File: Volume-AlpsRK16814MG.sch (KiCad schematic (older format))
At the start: 7 parts, among them P1 AB I/O, P2 CD I/O, P3 VD, P4 CTRL, U1 SN754410

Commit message: Flooded.
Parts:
- added P5: GND, mfk-AVA-20ga, symbol CONN_1
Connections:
- net GND: now also P5.1
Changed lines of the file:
@@
 63 98 05 E1 6B C4 72 91 8E EA 95 27 8C 4B 0B 6B 30 6B 95 2D 08 DF 47 79 14 D8 40 20 A9 90 96 2D
 E1 E7 3D C6 74 F3 E0 6E B9 00 E4 0E CC EC 2A 00 9E 03 F9 2E 43 53 93 3B E7 B1 3D FE 0F E4 2C B5
-B8 3A B8 3B 5D 00 00 00 00 49 45 4E 44 AE 42 60 82 C2 $EndBitmap
+B8 3A B8 3B 5D 00 00 00 00 49 45 4E 44 AE 42 60 82 AB $EndBitmap
 EndData
 $EndBitmap
@@
 Wire Wire Line
 	4700 6000 4700 6100
+$Comp
+L CONN_1 P5
+U 1 1 550D1AD1
+P 4350 6000
+F 0 "P5" H 4430 6000 40  0000 L CNN
+F 1 "GND" H 4350 6055 30  0001 C CNN
+F 2 "mfk-AVA-20ga" H 4350 6000 60  0001 C CNN
+F 3 "" H 4350 6000 60  0000 C CNN
+	1    4350 6000
+	-1   0    0    1
+$EndComp
+Wire Wire Line
+	4500 6000 4700 6000
 $EndSCHEMATC

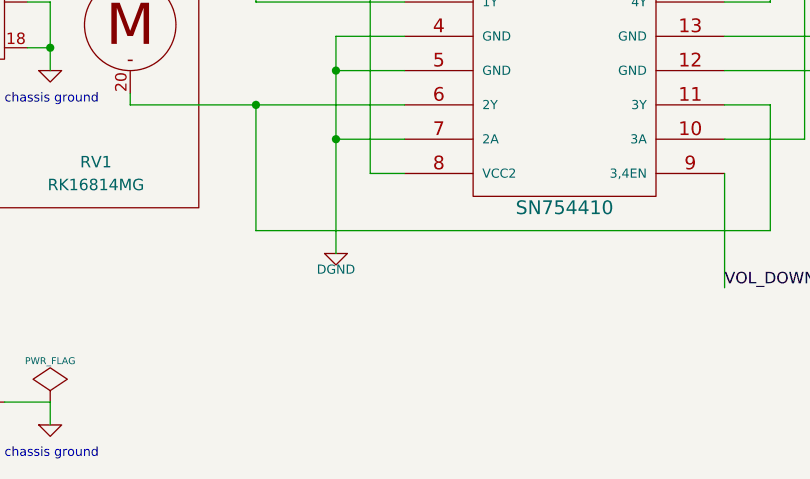
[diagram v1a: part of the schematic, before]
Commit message: Added bypass C to VCC2.
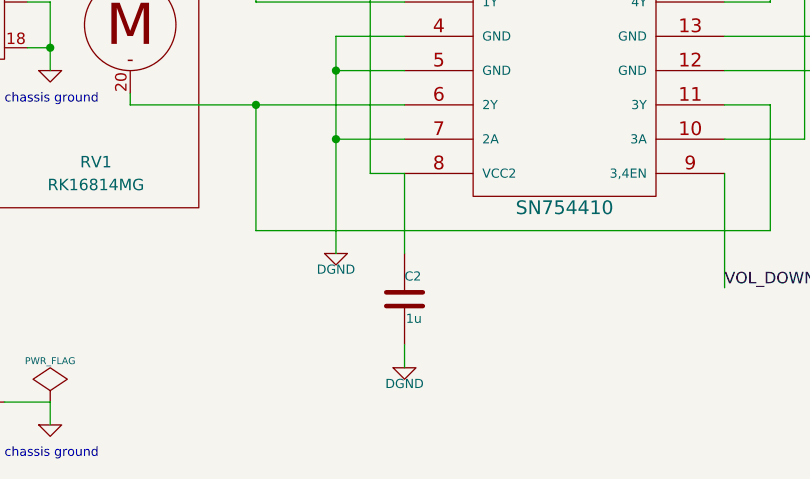
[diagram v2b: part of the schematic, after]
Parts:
- added C2: 1u, mfk-C_4.0_2.5_2.5_0.5, symbol C
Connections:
- net +5VD: now also C2.1
- net DGND: now also C2.2
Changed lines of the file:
@@
 63 98 05 E1 6B C4 72 91 8E EA 95 27 8C 4B 0B 6B 30 6B 95 2D 08 DF 47 79 14 D8 40 20 A9 90 96 2D
 E1 E7 3D C6 74 F3 E0 6E B9 00 E4 0E CC EC 2A 00 9E 03 F9 2E 43 53 93 3B E7 B1 3D FE 0F E4 2C B5
-B8 3A B8 3B 5D 00 00 00 00 49 45 4E 44 AE 42 60 82 AB $EndBitmap
+B8 3A B8 3B 5D 00 00 00 00 49 45 4E 44 AE 42 60 82 7C $EndBitmap
 EndData
 $EndBitmap
@@
 Wire Wire Line
 	4500 6000 4700 6000
+$Comp
+L C C2
+U 1 1 550D2A54
+P 6250 5550
+F 0 "C2" H 6250 5650 40  0000 L CNN
+F 1 "1u" H 6256 5465 40  0000 L CNN
+F 2 "mfk-C_4.0_2.5_2.5_0.5" H 6288 5400 30  0001 C CNN
+F 3 "TDK FK18X5R1A105K" H 6250 5550 60  0001 C CNN
+	1    6250 5550
+	1    0    0    -1
+$EndComp
+Wire Wire Line
+	6250 5350 6250 5000
+$Comp
+L DGND #PWR012
+U 1 1 550D2ACA
+P 6250 5850
+F 0 "#PWR012" H 6250 5850 40  0001 C CNN
+F 1 "DGND" H 6250 5780 40  0000 C CNN
+F 2 "" H 6250 5850 60  0000 C CNN
+F 3 "" H 6250 5850 60  0000 C CNN
+	1    6250 5850
+	1    0    0    -1
+$EndComp
+Wire Wire Line
+	6250 5850 6250 5750
 $EndSCHEMATC
